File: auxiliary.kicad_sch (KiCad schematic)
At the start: 75 parts, among them IC1 MAX1708EEE+, J4 JST_SH_1x4_SM04B-SRSS-TB-LF-SN, J5 SM06B-SRSS-TB(LF)(SN), J6 JST_SH_1x9_SM09B-SRSS-TB-LF-SN, Q1 BSS138AKA, U1 PCA9547_VQFN, U2 NTS0102_TSSOP

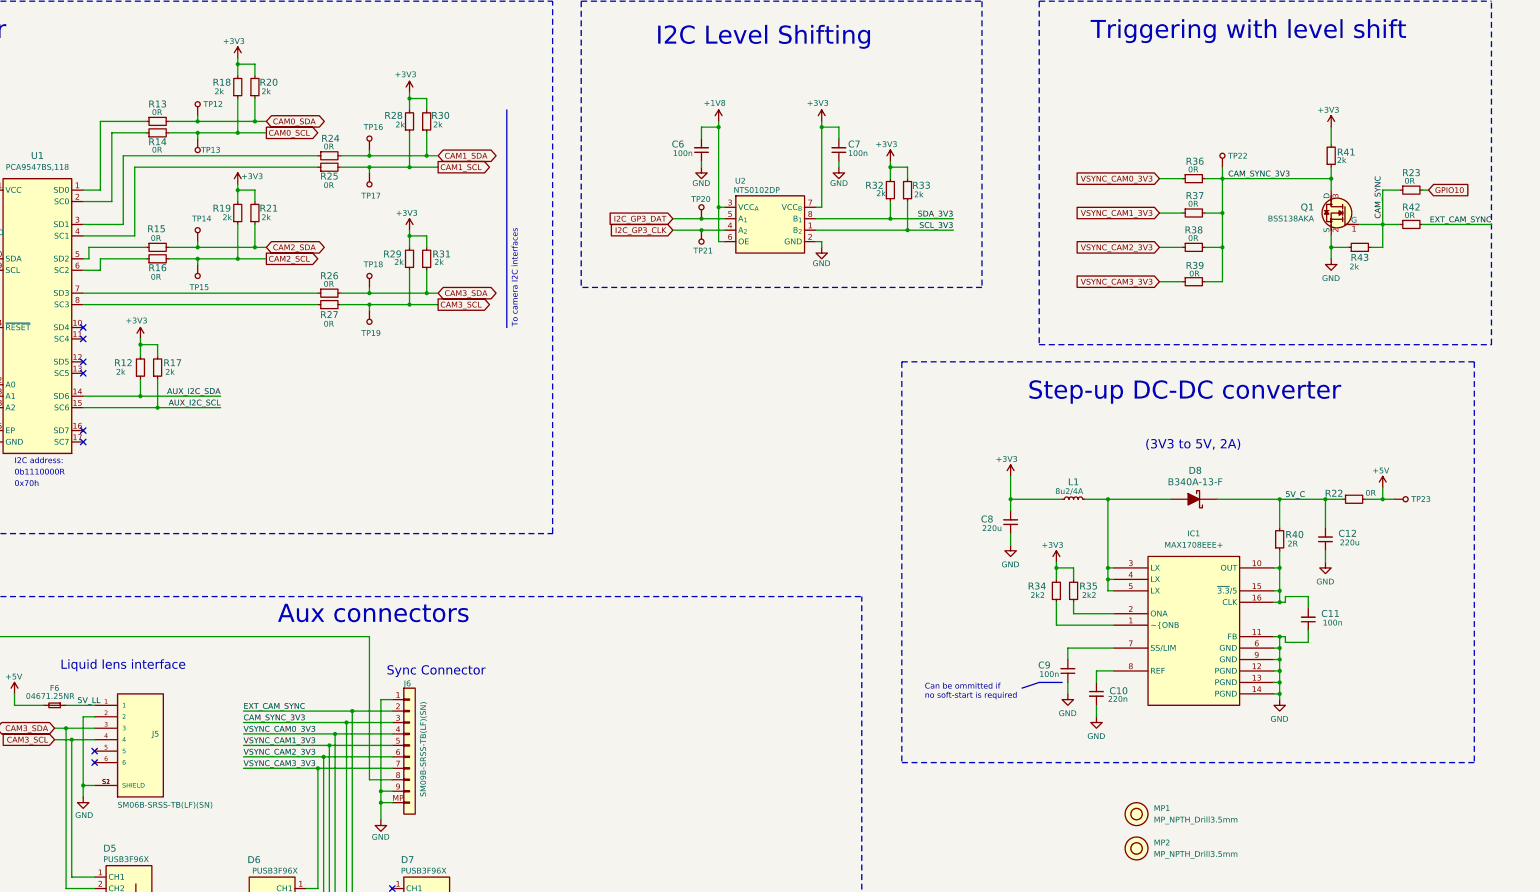
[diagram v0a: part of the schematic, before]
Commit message: [#60956] Update B340A-13-F,MAX1708EEE+ and TP_0_75mm from library
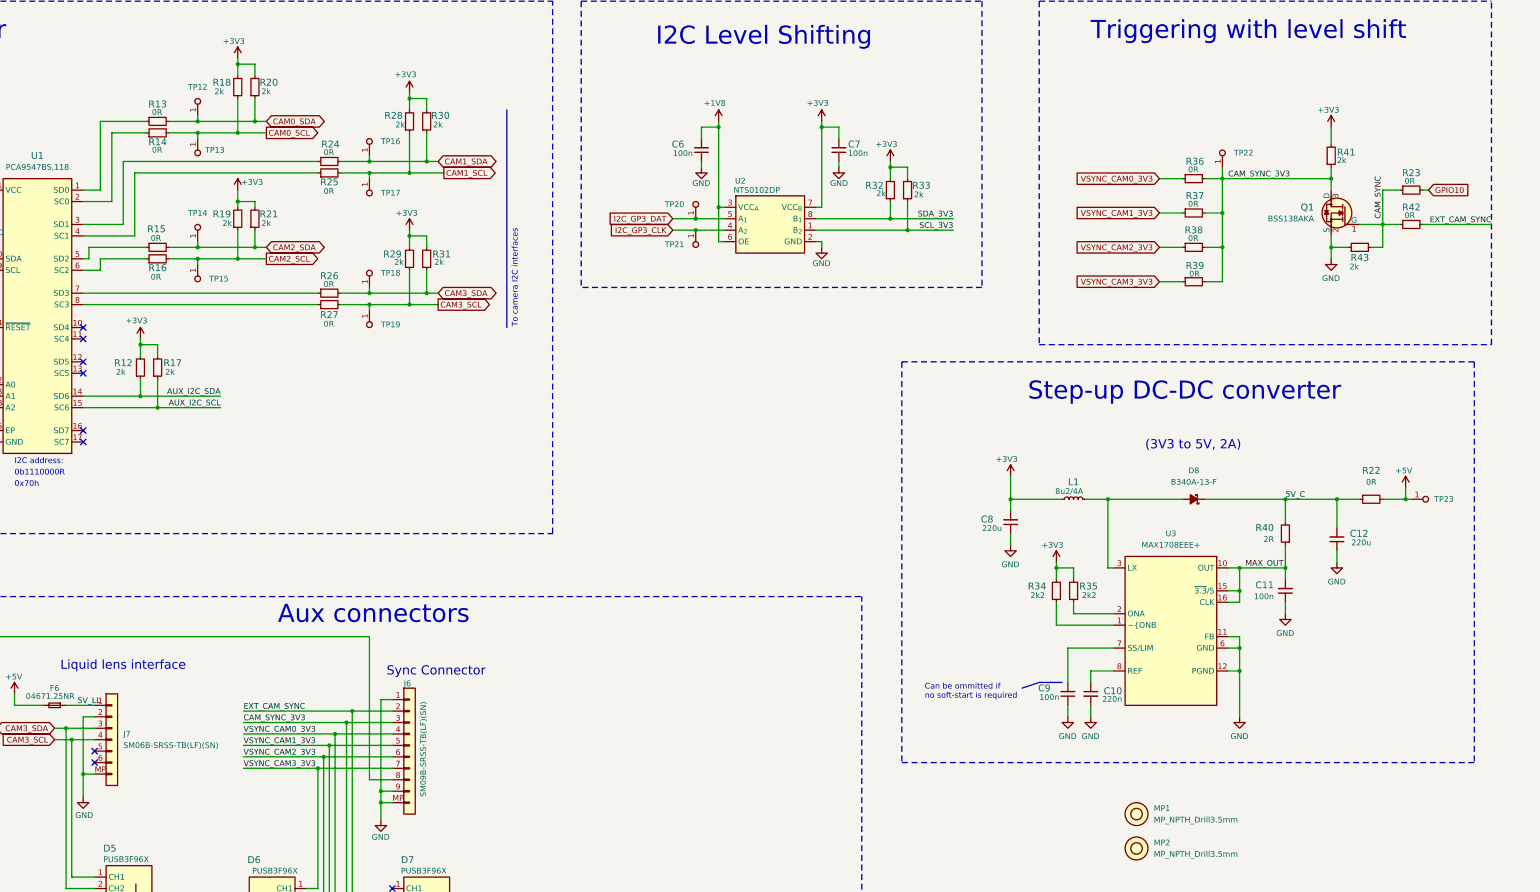
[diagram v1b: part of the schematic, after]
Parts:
- removed D8: B340A-13-F, antmicro-jetson-agx-csi-adapter-footprints:DO-214AC, symbol antmicro-jetson-agx-csi-adapter:B340A-13-F
- removed IC1: MAX1708EEE+, antmicro-jetson-agx-csi-adapter-footprints:QSOP-16_3.9x4.9mm_P0.635mm, symbol antmicro-jetson-agx-csi-adapter:MAX1708EEE+
- removed J5: SM06B-SRSS-TB(LF)(SN), antmicro-jetson-agx-csi-adapter-footprints:JST_SM06B-SRSS-TB(LF)(SN), symbol antmicro-jetson-agx-csi-adapter:SM06B-SRSS-TB(LF)(SN)
- removed TP18, TP19, TP20, TP21, TP22, TP23: TP_SMD_0_75MM, antmicro-jetson-agx-csi-adapter-footprints:Testpoint_smd_0_75mm, symbol antmicro-jetson-agx-csi-adapter:TP_SMD_0_75MM
- added D8: B340A-13-F, antmicro-footprints:D_SMA, symbol antmicroDiodesRectifiersSingle:B340A-13-F
- added J7: JST_SH_1x6_SM06B-SRSS-TB-LF-SN, antmicro-footprints:Conn_JST_SH_1x6_SM06B-SRSS-TB-LF-SN, symbol antmicroWire2BoardConnectors:JST_SH_1x6_SM06B-SRSS-TB-LF-SN
- added TP18, TP19, TP20, TP21, TP22, TP23: TP_0.75mm_SMD, antmicro-footprints:TP_SMD_0.75mm, symbol antmicroTestPoints:TP_0.75mm_SMD
- added U3: MAX1708EEE+, antmicro-footprints:QSOP-16_3.9x4.9mm_P0.635mm, symbol antmicroDCDCConverters:MAX1708EEE+
- TP12, TP13, TP14, TP15, TP16, TP17: value TP_SMD_0_75MM -> TP_0.75mm_SMD; footprint antmicro-jetson-agx-csi-adapter-footprints:Testpoint_smd_0_75mm -> antmicro-footprints:TP_SMD_0.75mm; symbol antmicro-jetson-agx-csi-adapter:TP_SMD_0_75MM -> antmicroTestPoints:TP_0.75mm_SMD; Author (none) -> Antmicro; License (none) -> Apache-2.0; Public (none) -> False; now left out of the parts list
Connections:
- net +5V: now also TP23.1
- net 5V_C: now also D8.1 (C)
- net 5V_LL: now also J7.1
- net CAM3_SCL: now also J7.4, TP19.1
- net CAM3_SDA: now also J7.3, TP18.1
- net CAM_SYNC_3V3: now also TP22.1
- net GND: now also J7.2, J7.MP, U3.11 (FB), U3.12 (PGND), U3.13 (PGND), U3.14 (PGND), U3.6 (GND), U3.9 (GND)
- net I2C_GP3_CLK: now also TP21.1
- net I2C_GP3_DAT: now also TP20.1
- net MAX_OUT: now reaches C11.2, R40.1
- net MAX_OUT: now also U3.10 (OUT), U3.15 (~{3.3}/5), U3.16 (CLK)
- net at R35.1: now also U3.2 (ONA)
- net at C9.2: now also U3.7 (SS/LIM)
- net at L1.2: now also D8.2 (A), U3.3 (LX), U3.4 (LX), U3.5 (LX)
- net at R34.1: now also U3.1 (~{ONB)
- net at C10.1: now also U3.8 (REF)
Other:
- moved on the sheet: C10, C11, C12, C9, R19, R21, R22, R24, R25, R40

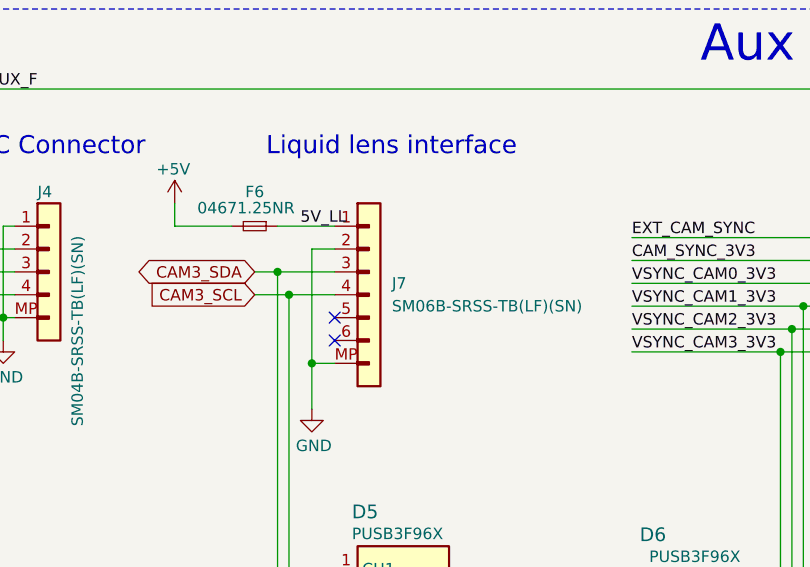
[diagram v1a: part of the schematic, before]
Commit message: [#60956] Allign PCB with SCH changes
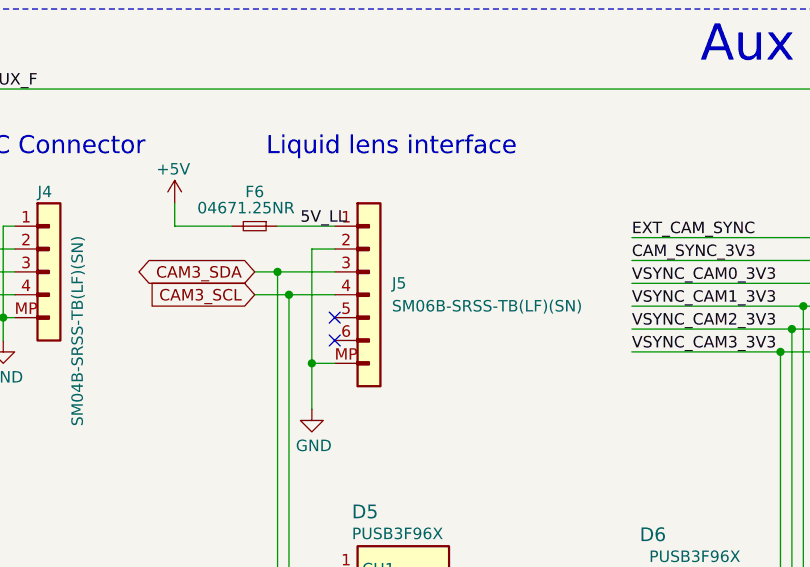
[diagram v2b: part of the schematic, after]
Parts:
- renumbered J7 to J5
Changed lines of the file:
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@@
   (symbol (lib_id "antmicroWire2BoardConnectors:JST_SH_1x6_SM06B-SRSS-TB-LF-SN") (at 88.9 180.34 0) (unit 1)
     (in_bom yes) (on_board yes) (dnp no) (fields_autoplaced)
-    (property "Reference" "J7" (at 95.25 186.69 0)
+    (property "Reference" "J5" (at 95.25 186.69 0)
       (effects (font (size 1.27 1.27) (thickness 0.15)) (justify left))
     )
@@
       (project "antmicro-jetson-agx-csi-adapter"
         (path "/670e9d2a-7922-4ce5-91a1-7b9e7947bcbf/979ab030-ea70-442d-80da-03811f49b178"
-          (reference "J7") (unit 1)
+          (reference "J5") (unit 1)
         )
       )
